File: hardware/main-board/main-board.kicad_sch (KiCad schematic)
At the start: 62 parts, among them J1 Barrel_Jack_Switch, J10 Conn_01x04, J11 Conn_01x04, J12 Conn_01x04, J13 USB_A, J14 USB_A, J15 USB_B, J16 USB_B, J17 USB_A, J18 USB_A, J19 USB_B, J2 Conn_02x05_Odd_Even, J20 USB_B, J3 Conn_02x05_Odd_Even, J4 Conn_01x06, J5 Conn_02x05_Odd_Even, J6 Conn_02x05_Odd_Even, J7 Conn_01x05, J8 Conn_02x03_Odd_Even, J9 8P8C_LED, Q1 KSP43BU, Q2 KSP43BU, Q3 KSP43BU, Q4 KSP43BU, Q5 KSP43BU, Q6 KSP43BU, Q7 KSP43BU, Q8 KSP43BU, U1 LM317_TO-220, U2 R-78E5.0-0.5, U3 LF33_TO220, U4 ASSR-1218, U5 ASSR-1218, U6 ASSR-1218, U7 Teensy4.1, U8 ASSR-1218, U9 ASSR-1218

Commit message: Complete main board schematic
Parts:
- removed U4, U5, U6, U8, U9: ASSR-1218, Package_SO:SO-4_4.4x4.3mm_P2.54mm, symbol Relay_SolidState:ASSR-1218
- added R5, R6: 0R, Resistor_THT:R_Axial_DIN0207_L6.3mm_D2.5mm_P10.16mm_Horizontal, symbol Device:R
- added U4: Omron_G3VM-41AY1, Package_DIP:DIP-4_W7.62mm, symbol Relay_SolidState:Omron_G3VM-41AY1
- added U5, U6, U8, U9: Omron_G3VM-61A1, Package_DIP:DIP-4_W7.62mm, symbol Relay_SolidState:Omron_G3VM-61A1
- C1, D1: footprint (none) -> Diode_THT:D_DO-34_SOD68_P10.16mm_Horizontal
- C2, C4: footprint (none) -> Capacitor_SMD:C_0805_2012Metric_Pad1.18x1.45mm_HandSolder
- C3, C7: footprint (none) -> Capacitor_THT:C_Disc_D4.7mm_W2.5mm_P5.00mm
- C5, C6: footprint (none) -> Capacitor_THT:CP_Radial_D5.0mm_P2.00mm
- J1: footprint (none) -> Connector_BarrelJack:BarrelJack_RS-PRO_12V1A_14.5mmL
- J10, J11, J12: footprint (none) -> Connector_PinHeader_2.54mm:PinHeader_1x04_P2.54mm_Vertical
- J13, J14, J17, J18: footprint (none) -> Connector_USB:USB_A_ASSMANN_A-USB-E-R
- J15, J16, J19, J20: footprint (none) -> Connector_USB:USB_B_ASSMANN_A-USBSB
- J2, J3, J5, J6: footprint (none) -> Connector_PinHeader_2.54mm:PinHeader_AWHW_2x05_P2.54mm_Vertical
- J4: footprint (none) -> Connector_PinHeader_2.54mm:PinHeader_1x06_P2.54mm_Vertical
- J7: footprint (none) -> Connector_PinHeader_2.54mm:PinHeader_1x05_P2.54mm_Vertical
- J8: footprint (none) -> Connector_PinHeader_2.00mm:PinHeader_2x03_P2.00mm_Vertical
- J9: footprint (none) -> Connector_RJ:RJ45_Cetus_J1B1211CCD_Horizontal
- R1, R2, R3, R4: footprint (none) -> Resistor_THT:R_Axial_DIN0207_L6.3mm_D2.5mm_P10.16mm_Horizontal
- R10: renamed from R8; footprint (none) -> Resistor_THT:R_Axial_DIN0207_L6.3mm_D2.5mm_P10.16mm_Horizontal
- R11: renamed from R9; footprint (none) -> Resistor_THT:R_Axial_DIN0207_L6.3mm_D2.5mm_P10.16mm_Horizontal
- R12: renamed from R10; footprint (none) -> Resistor_THT:R_Axial_DIN0207_L6.3mm_D2.5mm_P10.16mm_Horizontal
- R13: renamed from R11; footprint (none) -> Resistor_THT:R_Axial_DIN0207_L6.3mm_D2.5mm_P10.16mm_Horizontal
- R14: renamed from R12; footprint (none) -> Resistor_THT:R_Axial_DIN0207_L6.3mm_D2.5mm_P10.16mm_Horizontal
- R15: renamed from R13; footprint (none) -> Resistor_THT:R_Axial_DIN0207_L6.3mm_D2.5mm_P10.16mm_Horizontal
- R16: renamed from R14; footprint (none) -> Resistor_THT:R_Axial_DIN0207_L6.3mm_D2.5mm_P10.16mm_Horizontal
- R17: renamed from R15; footprint (none) -> Resistor_THT:R_Axial_DIN0207_L6.3mm_D2.5mm_P10.16mm_Horizontal
- R18: renamed from R16; footprint (none) -> Resistor_THT:R_Axial_DIN0207_L6.3mm_D2.5mm_P10.16mm_Horizontal
- R19: renamed from R17; footprint (none) -> Resistor_THT:R_Axial_DIN0207_L6.3mm_D2.5mm_P10.16mm_Horizontal
- R7: renamed from R5; footprint (none) -> Resistor_THT:R_Axial_DIN0207_L6.3mm_D2.5mm_P10.16mm_Horizontal
- R8: renamed from R6; footprint (none) -> Resistor_THT:R_Axial_DIN0207_L6.3mm_D2.5mm_P10.16mm_Horizontal
- R9: renamed from R7; footprint (none) -> Resistor_THT:R_Axial_DIN0207_L6.3mm_D2.5mm_P10.16mm_Horizontal
- U7: footprint (none) -> Package_DIP:DIP-48_W15.24mm
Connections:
- net +12V: now also R5.1
- net GND: now also R6.1; no longer J12.3 (Pin_3), J12.4 (Pin_4)
- net at J14.1 (VBUS): now also U6.3
- net at J16.1 (VBUS): now also U6.4
- net at Q3.3 (C): now also U4.2
- net at R19.2: now also U9.1
- net at J19.1 (VBUS): now also U8.4
- net at Q8.3 (C): now also U9.2
- net at J18.1 (VBUS): now also U9.3
- net at J20.1 (VBUS): now also U9.4
- net at J12.1 (Pin_1): now also U4.3
- net at J15.1 (VBUS): now also U5.4
- net at R18.2: now also U8.1
- net at R15.2: now also U6.1
- net at Q6.3 (C): now also U6.2
- net at Q7.3 (C): now also U8.2
- net at R14.2: now also U5.1
- net at Q5.3 (C): now also U5.2
- net at J13.1 (VBUS): now also U5.3
- net at R8.2: now also U4.1
- net at J17.1 (VBUS): now also U8.3
- new net +12VA: R5.2, U4.4
- new net GNDA: J12.3 (Pin_3), J12.4 (Pin_4), R6.2

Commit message: PCB updates
Alter schematic to use ESP32 and add final PCB for USB enable/disables
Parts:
- removed J4: Conn_01x06, Connector_PinHeader_2.54mm:PinHeader_1x06_P2.54mm_Vertical, symbol Connector_Generic:Conn_01x06
- removed J8: Conn_02x03_Odd_Even, Connector_PinHeader_2.00mm:PinHeader_2x03_P2.00mm_Vertical, symbol Connector_Generic:Conn_02x03_Odd_Even
- removed J9: 8P8C_LED, Connector_RJ:RJ45_Cetus_J1B1211CCD_Horizontal, symbol Connector:8P8C_LED
- removed U7: Teensy4.1, Package_DIP:DIP-48_W15.24mm, symbol teensy:Teensy4.1
- added C8: 33pF, Capacitor_THT:C_Disc_D4.7mm_W2.5mm_P5.00mm, symbol Device:C
- added R20, R23: 3.3K, Resistor_THT:R_Axial_DIN0207_L6.3mm_D2.5mm_P10.16mm_Horizontal, symbol Device:R
- added R21, R22: 3.9K, Resistor_THT:R_Axial_DIN0207_L6.3mm_D2.5mm_P10.16mm_Horizontal, symbol Device:R
- added U10, U9: MCP23016_SS, Package_DIP:DIP-28_W7.62mm, symbol Interface_Expansion:MCP23016_SS
- added U11: ESP32-PoE-ISO, symbol MCU_Espressif:ESP32-PoE-ISO
- C1: footprint Diode_THT:D_DO-34_SOD68_P10.16mm_Horizontal -> Capacitor_THT:C_Disc_D4.7mm_W2.5mm_P5.00mm
- C7: value 0.1uF -> 33pF
- renumbered J11 to J10, J12 to J11, J15 to J12, J16 to J13, J17 to J14, J18 to J15, J19 to J16, J20 to J17, J5 to J4, J6 to J5, J7 to J6, J13 to J7, J14 to J8, J10 to J9, Q5 to Q3, Q6 to Q4, Q3 to Q5, Q4 to Q6, R14 to R10, R15 to R11, R8 to R12, R9 to R13, R10 to R14, R11 to R15, R12 to R5, R13 to R6, R5 to R7, R6 to R8, R7 to R9, U5 to U4, U6 to U5, U4 to U6, U8 to U7, U9 to U8
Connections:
- net USB_GND_1 is gone; now on net GND: J12.5 (Shield), J7.5 (Shield)
- net USB_GND_2 is gone; now on net GND: J14.5 (Shield), J16.5 (Shield)
- net USB_GND_3 is gone; now on net GND: J13.5 (Shield), J8.5 (Shield)
- net USB_GND_4 is gone; now on net GND: J15.5 (Shield), J17.5 (Shield)
- net +3V3: now also R20.2, R21.2, R22.2, R23.2, U10.16 (A0), U10.20 (VDD), U9.20 (VDD)
- net GND: now also C7.2, J12.4 (GND), J13.4 (GND), J14.4 (GND), J15.4 (GND), J16.4 (GND), J17.4 (GND), J7.4 (GND), J8.4 (GND), C8.2, U10.1 (VSS), U10.17 (A1), U10.18 (A2), U10.19 (VSS), U10.8 (VSS), U11.3 (GND), U9.1 (VSS), U9.16 (A0), U9.17 (A1), U9.18 (A2), U9.19 (VSS), U9.8 (VSS)
- net IO_0: now also U11.9 (GPIO4)
- net IO_1: now also U11.10 (GPIO5)
- net IR_BTN: now also U10.11 (GP1.5)
- net IR_LED: now also U9.13 (GP1.7)
- net IR_RLY_IN: now also U10.7 (GP1.4)
- net IR_RLY_OUT: now also U9.12 (GP1.6)
- net LED_0: now also U10.12 (GP1.6)
- net LED_1: now also U10.13 (GP1.7)
- net P1_LED_A: now also U9.21 (GP0.0)
- net P1_LED_B: now also U9.22 (GP0.1)
- net P1_LED_C: now also U9.23 (GP0.2)
- net P1_SW_0: now also U10.21 (GP0.0)
- net P1_SW_1: now also U10.22 (GP0.1)
- net P1_SW_2: now also U10.23 (GP0.2)
- net P2_LED_A: now also U9.24 (GP0.3)
- net P2_LED_B: now also U9.25 (GP0.4)
- net P2_LED_C: now also U9.26 (GP0.5)
- net P2_SW_0: now also U10.24 (GP0.3)
- net P2_SW_1: now also U10.25 (GP0.4)
- net P2_SW_2: now also U10.26 (GP0.5)
- net P3_LED_A: now also U9.27 (GP0.6)
- net P3_LED_B: now also U9.28 (GP0.7)
- net P3_LED_C: now also U9.2 (GP1.0)
- net P3_SW_0: now also U10.27 (GP0.6)
- net P3_SW_1: now also U10.28 (GP0.7)
- net P3_SW_2: now also U10.2 (GP1.0)
- net P4_LED_A: now also U9.3 (GP1.1)
- net P4_LED_B: now also U9.4 (GP1.2)
- net P4_LED_C: now also U9.5 (GP1.3)
- net P4_SW_0: now also U10.3 (GP1.1)
- net P4_SW_1: now also U10.4 (GP1.2)
- net P4_SW_2: now also U10.5 (GP1.3)
- net USB_EN_A: now also U9.7 (GP1.4)
- net USB_EN_B: now also U9.11 (GP1.5)
- net at C7.1: now also R21.1, U9.9 (CLK)
- new net: C8.1, R22.1, U10.9 (CLK)
- new net I2C_SCL: R20.1, U10.14 (SCL), U11.16 (GPIO33), U9.14 (SCL)
- new net I2C_SDA: R23.1, U10.15 (SDA), U11.15 (GPIO32), U9.15 (SDA)
- no-connect marks 33 -> 12
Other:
- note added: "I2C Expansion modules"
- note removed: "DOES THIS OFFER ENOUGH INPUT PROTECTION??? HMMM"
- note removed: "Magjack Connector"
- note removed: "PHY output connected from header on devboard to header - see connection to magjack"
- note removed: "RS232 Output Connector"
- note removed: "RX TX CTS RTS +5V GND"
- moved on the sheet: J11, J12, J13, J14, J15, J16, J17, J7, J8, Q3, Q4, Q5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

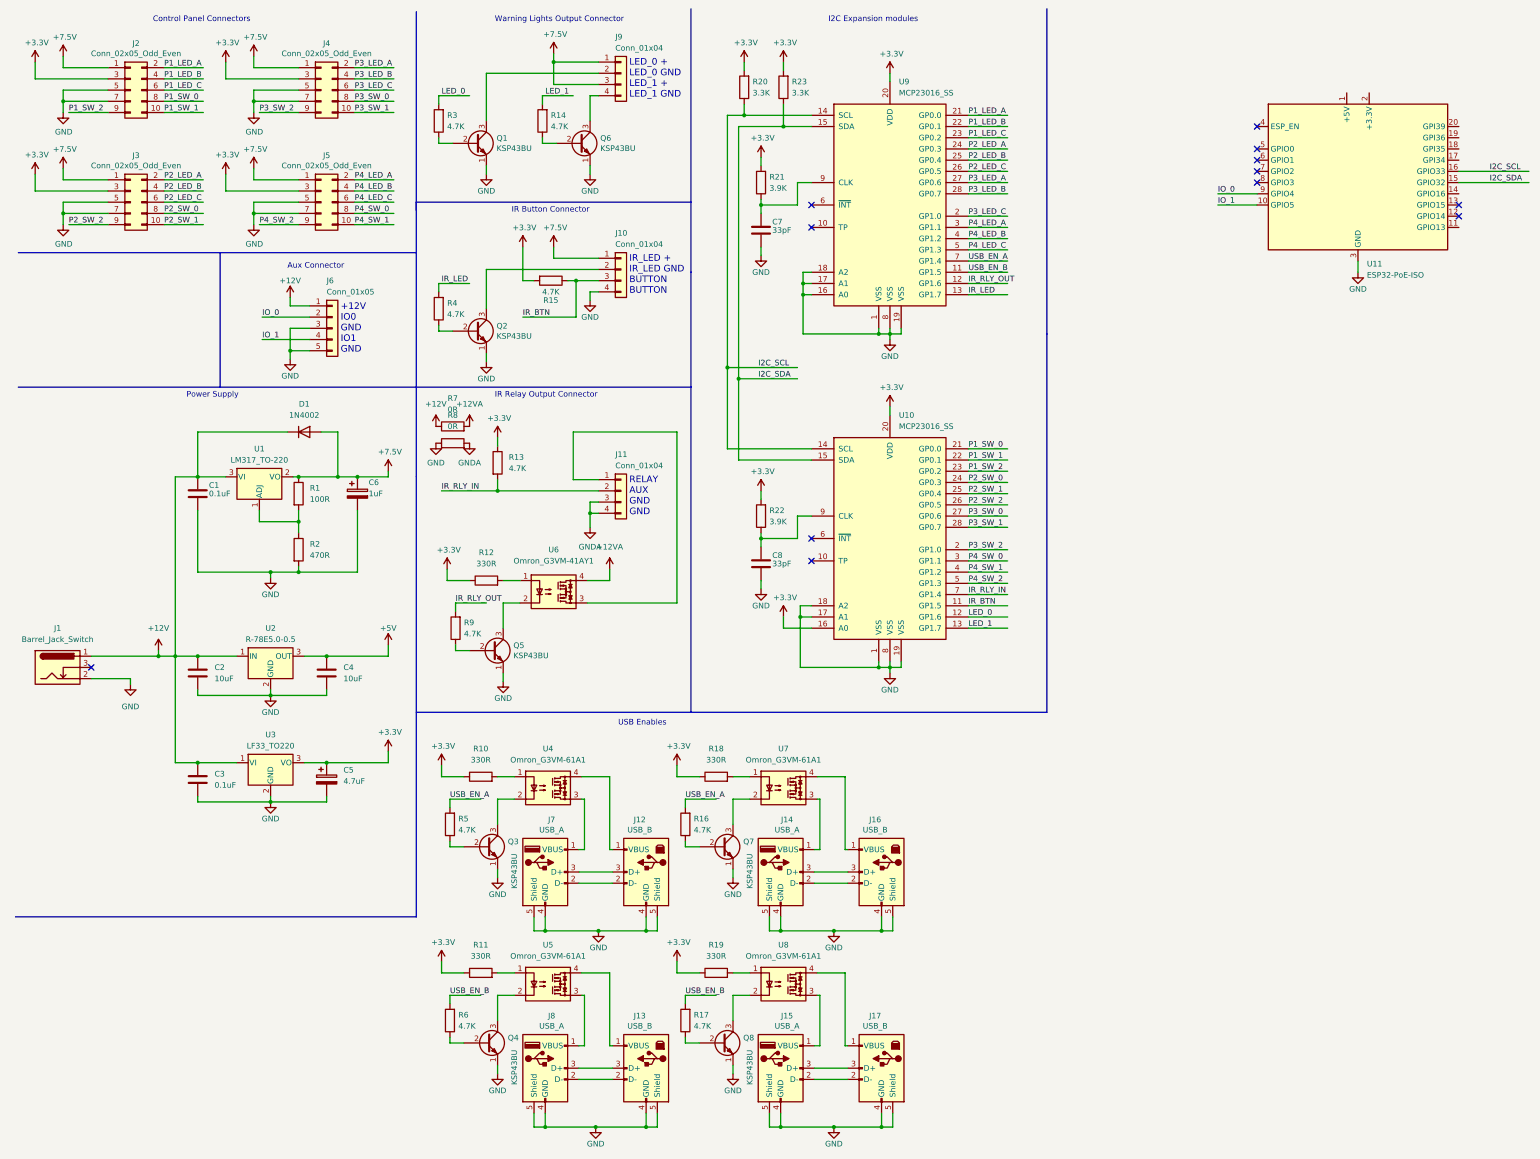
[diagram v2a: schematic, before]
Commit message: Rev A mainboard PCB
Altered to split IR relay off into isolated section
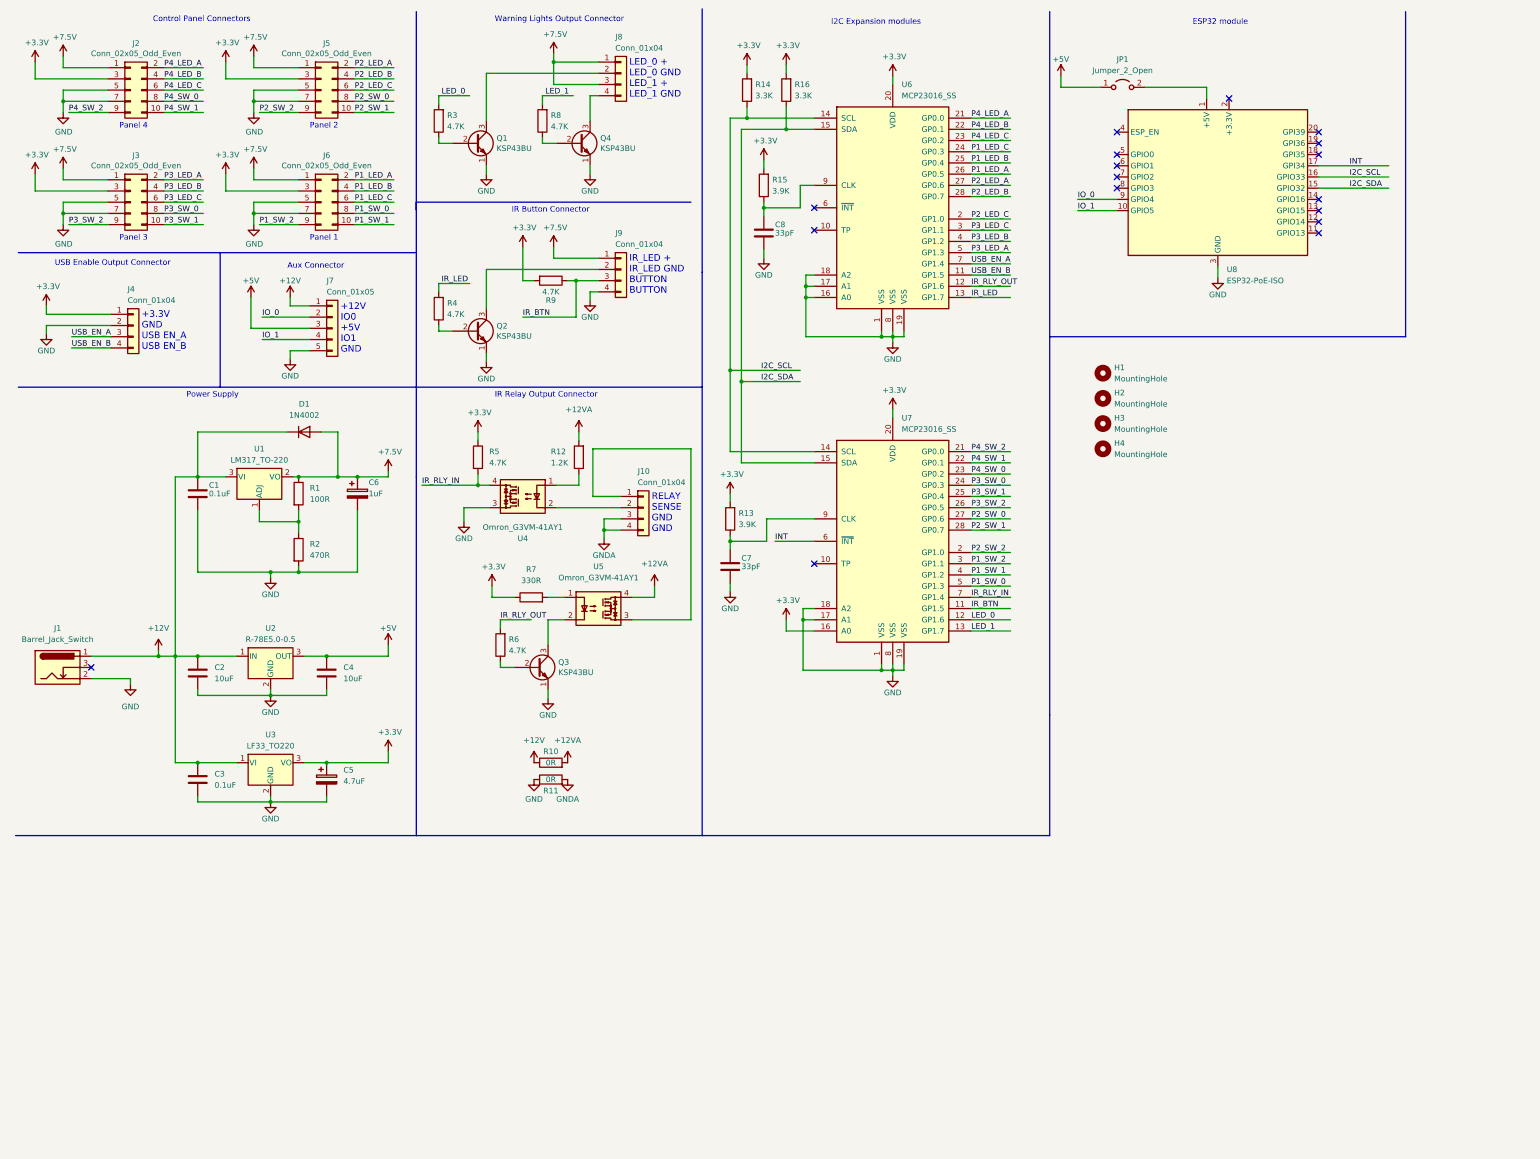
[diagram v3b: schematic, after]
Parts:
- removed J12, J13, J16, J17: USB_B, Connector_USB:USB_B_ASSMANN_A-USBSB, symbol Connector:USB_B
- removed J14, J15, J7, J8: USB_A, Connector_USB:USB_A_ASSMANN_A-USB-E-R, symbol Connector:USB_A
- removed Q3, Q4, Q7, Q8: KSP43BU, Package_TO_SOT_THT:TO-92_Inline, symbol Device:Q_NPN_EBC
- removed R10, R11, R18, R19: 330R, Resistor_THT:R_Axial_DIN0207_L6.3mm_D2.5mm_P10.16mm_Horizontal, symbol Device:R
- removed R16, R17, R5, R6: 4.7K, Resistor_THT:R_Axial_DIN0207_L6.3mm_D2.5mm_P10.16mm_Horizontal, symbol Device:R
- removed U4, U5, U7, U8: Omron_G3VM-61A1, Package_DIP:DIP-4_W7.62mm, symbol Relay_SolidState:Omron_G3VM-61A1
- added H1, H2, H3, H4: MountingHole, MountingHole:MountingHole_4.3mm_M4, symbol Mechanical:MountingHole
- added J4: Conn_01x04, Connector_PinHeader_2.54mm:PinHeader_1x04_P2.54mm_Vertical, symbol Connector_Generic:Conn_01x04
- added JP1: Jumper_2_Open, Jumper:SolderJumper-2_P1.3mm_Open_TrianglePad1.0x1.5mm, symbol Jumper:Jumper_2_Open
- added R12: 1.2K, Resistor_THT:R_Axial_DIN0207_L6.3mm_D2.5mm_P10.16mm_Horizontal, symbol Device:R
- added U4: Omron_G3VM-41AY1, Package_DIP:DIP-4_W7.62mm, symbol Relay_SolidState:Omron_G3VM-41AY1
- C2, C4: footprint Capacitor_SMD:C_0805_2012Metric_Pad1.18x1.45mm_HandSolder -> Capacitor_SMD:C_1210_3225Metric_Pad1.33x2.70mm_HandSolder
- U8: renamed from U11; footprint (none) -> Module:Olimex_ESP32_PoE_ISO
- renumbered C8 to C7, C7 to C8, J11 to J10, J4 to J5, J5 to J6, J6 to J7, J9 to J8, J10 to J9, Q5 to Q3, Q6 to Q4, R7 to R10, R8 to R11, R22 to R13, R20 to R14, R21 to R15, R23 to R16, R13 to R5, R9 to R6, R12 to R7, R14 to R8, R15 to R9, U6 to U5, U9 to U6, U10 to U7
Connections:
- net +12VA: now also R12.2
- net +3V3: now also J4.1 (Pin_1)
- net +5V: now also J7.3 (Pin_3), JP1.1 (A)
- net GND: now also J4.2 (Pin_2), U4.3; no longer J7.3 (Pin_3)
- net IR_RLY_IN: now also U4.4; no longer J10.2 (Pin_2)
- net P1_LED_A: now also J6.2 (Pin_2), U6.26 (GP0.5); no longer J2.2 (Pin_2), U6.21 (GP0.0)
- net P1_LED_B: now also J6.4 (Pin_4), U6.25 (GP0.4); no longer J2.4 (Pin_4), U6.22 (GP0.1)
- net P1_LED_C: now also J6.6 (Pin_6), U6.24 (GP0.3); no longer J2.6 (Pin_6), U6.23 (GP0.2)
- net P1_SW_0: now also J6.8 (Pin_8), U7.5 (GP1.3); no longer J2.8 (Pin_8), U7.21 (GP0.0)
- net P1_SW_1: now also J6.10 (Pin_10), U7.4 (GP1.2); no longer J2.10 (Pin_10), U7.22 (GP0.1)
- net P1_SW_2: now also J6.9 (Pin_9), U7.3 (GP1.1); no longer J2.9 (Pin_9), U7.23 (GP0.2)
- net P2_LED_A: now also J5.2 (Pin_2), U6.27 (GP0.6); no longer J3.2 (Pin_2), U6.24 (GP0.3)
- net P2_LED_B: now also J5.4 (Pin_4), U6.28 (GP0.7); no longer J3.4 (Pin_4), U6.25 (GP0.4)
- net P2_LED_C: now also J5.6 (Pin_6), U6.2 (GP1.0); no longer J3.6 (Pin_6), U6.26 (GP0.5)
- net P2_SW_0: now also J5.8 (Pin_8), U7.27 (GP0.6); no longer J3.8 (Pin_8), U7.24 (GP0.3)
- net P2_SW_1: now also J5.10 (Pin_10), U7.28 (GP0.7); no longer J3.10 (Pin_10), U7.25 (GP0.4)
- net P2_SW_2: now also J5.9 (Pin_9), U7.2 (GP1.0); no longer J3.9 (Pin_9), U7.26 (GP0.5)
- net P3_LED_A: now also J3.2 (Pin_2), U6.5 (GP1.3); no longer J5.2 (Pin_2), U6.27 (GP0.6)
- net P3_LED_B: now also J3.4 (Pin_4), U6.4 (GP1.2); no longer J5.4 (Pin_4), U6.28 (GP0.7)
- net P3_LED_C: now also J3.6 (Pin_6), U6.3 (GP1.1); no longer J5.6 (Pin_6), U6.2 (GP1.0)
- net P3_SW_0: now also J3.8 (Pin_8), U7.24 (GP0.3); no longer J5.8 (Pin_8), U7.27 (GP0.6)
- net P3_SW_1: now also J3.10 (Pin_10), U7.25 (GP0.4); no longer J5.10 (Pin_10), U7.28 (GP0.7)
- net P3_SW_2: now also J3.9 (Pin_9), U7.26 (GP0.5); no longer J5.9 (Pin_9), U7.2 (GP1.0)
- net P4_LED_A: now also J2.2 (Pin_2), U6.21 (GP0.0); no longer J6.2 (Pin_2), U6.3 (GP1.1)
- net P4_LED_B: now also J2.4 (Pin_4), U6.22 (GP0.1); no longer J6.4 (Pin_4), U6.4 (GP1.2)
- net P4_LED_C: now also J2.6 (Pin_6), U6.23 (GP0.2); no longer J6.6 (Pin_6), U6.5 (GP1.3)
- net P4_SW_0: now also J2.8 (Pin_8), U7.23 (GP0.2); no longer J6.8 (Pin_8), U7.3 (GP1.1)
- net P4_SW_1: now also J2.10 (Pin_10), U7.22 (GP0.1); no longer J6.10 (Pin_10), U7.4 (GP1.2)
- net P4_SW_2: now also J2.9 (Pin_9), U7.21 (GP0.0); no longer J6.9 (Pin_9), U7.5 (GP1.3)
- net USB_EN_A: now also J4.3 (Pin_3)
- net USB_EN_B: now also J4.4 (Pin_4)
- net at U8.1 (+5V): now also JP1.2 (B)
- net INT: now reaches U8.17 (GPI34)
- net INT: now also U7.6 (~{INT})
- new net: J10.2 (Pin_2), U4.2
- new net: R12.1, U4.1
- no-connect marks 12 -> 17
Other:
- note added: "+12V IO0 +5V IO1 GND"
- note added: "+3.3V GND USB EN_A USB EN_B"
- note added: "ESP32 module"
- note added: "Panel 1"
- note added: "Panel 2"
- note added: "Panel 3"
- note added: "Panel 4"
- note added: "RELAY SENSE GND GND"
- note added: "USB Enable Output Connector"
- note removed: "+12V IO0 GND IO1 GND"
- note removed: "RELAY AUX GND GND"
- note removed: "USB Enables"
- title: (none) -> SM Desk Video switcher mainboard
- moved on the sheet: C7, C8, J10, Q3, R10, R11, R13, R14, R15, R16, R5, R6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
